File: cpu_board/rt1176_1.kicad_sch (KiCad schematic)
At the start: 40 parts, among them SW1 SWITCH_SMT4.6X2.8, U2 MIMXRT1176

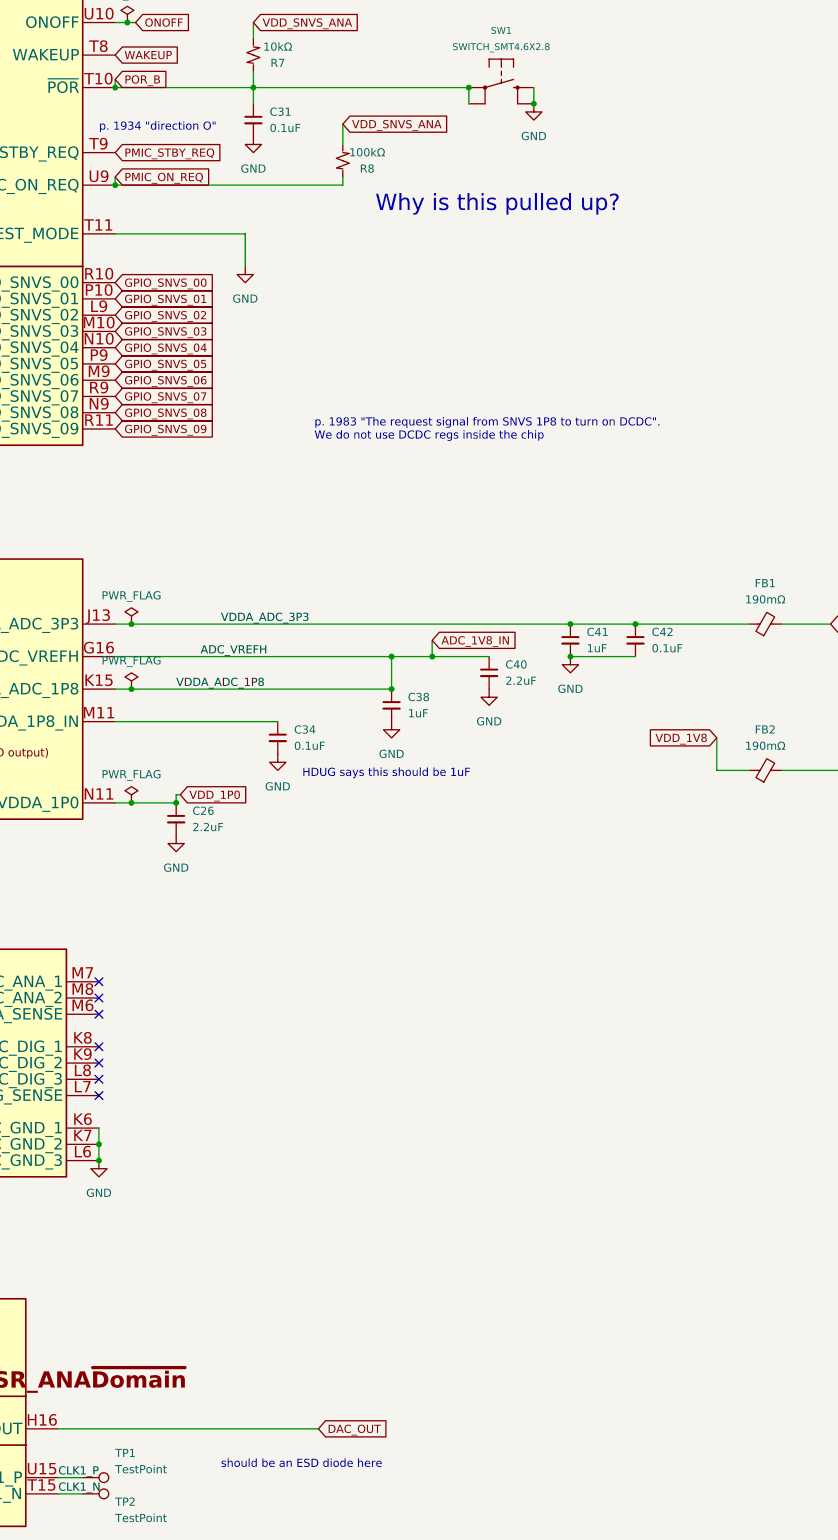
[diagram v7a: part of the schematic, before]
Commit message: move level shifter to top
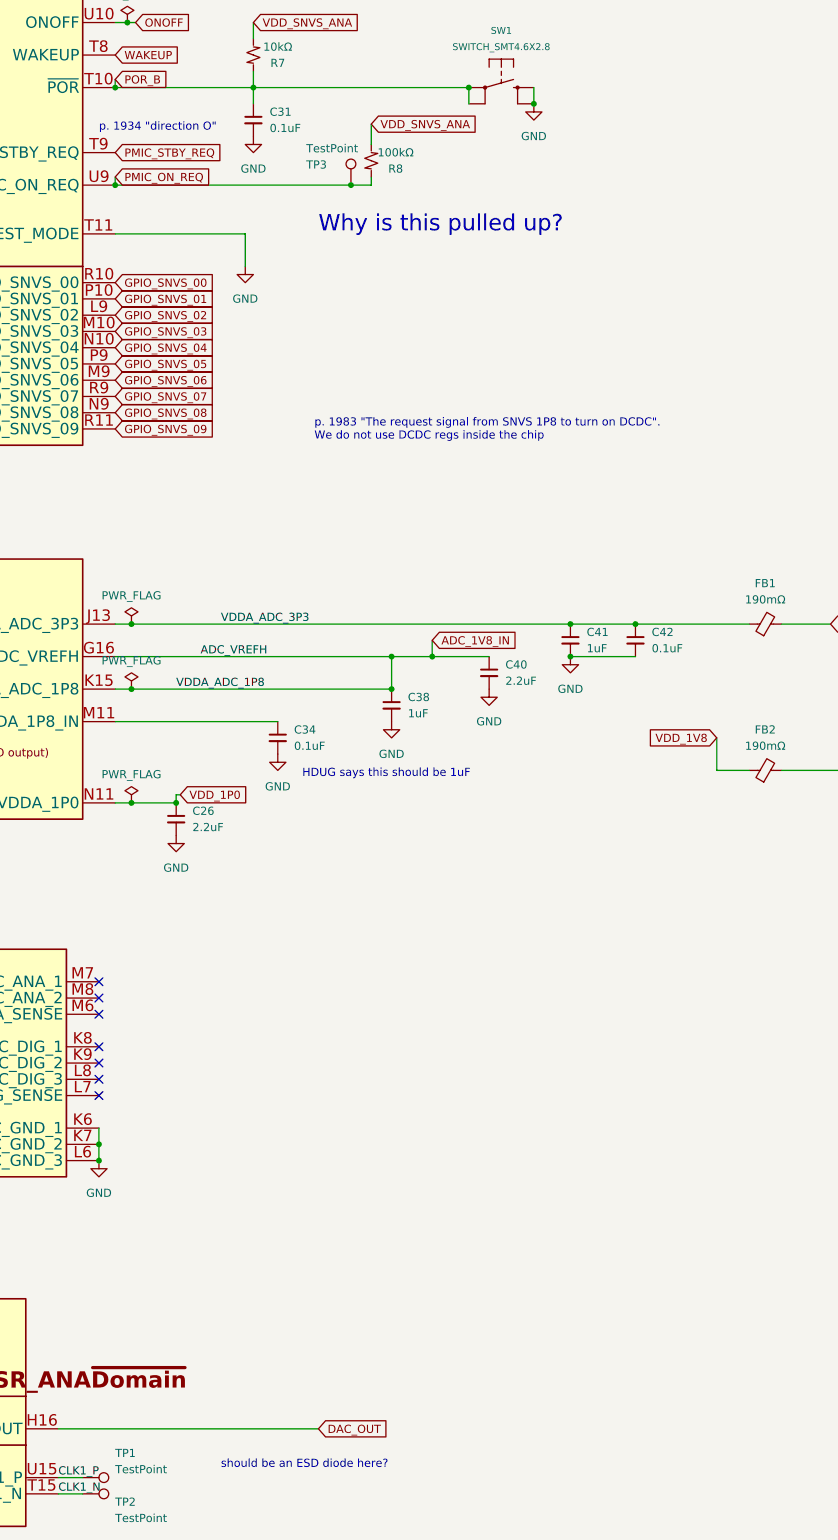
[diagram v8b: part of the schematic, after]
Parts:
- added TP3: TestPoint, TestPoint:TestPoint_Pad_1.0x1.0mm, symbol Connector:TestPoint
- C4: footprint adcs:Perfect_0402 -> Capacitor_SMD:C_0603_1608Metric
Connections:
- net PMIC_ON_REQ: now also TP3.1
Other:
- note added: "should be an ESD diode here?"
- note removed: "should be an ESD diode here"
- moved on the sheet: R8
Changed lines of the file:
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@@
   (junction (at 192.405 40.64) (diameter 0) (color 0 0 0 0)
   )
+  (junction (at 285.75 60.96) (diameter 0) (color 0 0 0 0)
+  )
   (junction (at 35.56 220.98) (diameter 0) (color 0 0 0 0)
   )
@@
     (stroke (width 0) (type default))
   )
+  (wire (pts (xy 248.92 60.96) (xy 285.75 60.96))
+    (stroke (width 0) (type default))
+  )
+  (wire (pts (xy 285.75 60.96) (xy 288.925 60.96))
+    (stroke (width 0) (type default))
+  )
   (wire (pts (xy 193.04 154.94) (xy 193.04 157.48))
     (stroke (width 0) (type default))
@@
     (stroke (width 0) (type default))
   )
-  (wire (pts (xy 284.48 59.69) (xy 284.48 60.96))
+  (wire (pts (xy 288.925 59.69) (xy 288.925 60.96))
     (stroke (width 0) (type default))
   )
@@
     (stroke (width 0) (type default))
   )
-  (wire (pts (xy 284.48 51.435) (xy 284.48 54.61))
+  (wire (pts (xy 288.925 51.435) (xy 288.925 54.61))
     (stroke (width 0) (type default))
   )
@@
     (stroke (width 0) (type default))
   )
-  (wire (pts (xy 248.92 60.96) (xy 284.48 60.96))
-    (stroke (width 0) (type default))
-  )
   (wire (pts (xy 251.46 129.54) (xy 320.04 129.54))
     (stroke (width 0) (type default))
@@
     (effects (font (size 1.27 1.27)) (justify left bottom))
   )
-  (text "should be an ESD diode here\n" (at 265.43 261.62 0)
+  (text "should be an ESD diode here?\n" (at 265.43 261.62 0)
     (effects (font (size 1.27 1.27)) (justify left bottom))
   )
@@
     (effects (font (size 1.27 1.27)) (justify left bottom))
   )
-  (text "Why is this pulled up?" (at 289.56 65.405 0)
+  (text "Why is this pulled up?" (at 280.67 68.58 0)
     (effects (font (size 2.54 2.54) (color 255 0 0 1)) (justify left bottom))
   )
@@
     )
   )
-  (global_label "VDD_SNVS_ANA" (shape input) (at 284.48 51.435 0) (fields_autoplaced)
+  (global_label "VDD_SNVS_ANA" (shape input) (at 288.925 51.435 0) (fields_autoplaced)
     (effects (font (size 1.27 1.27)) (justify left))
-    (property "Intersheetrefs" "${INTERSHEET_REFS}" (at 301.3748 51.435 0)
+    (property "Intersheetrefs" "${INTERSHEET_REFS}" (at 305.8198 51.435 0)
       (effects (font (size 1.27 1.27)) (justify left) hide)
     )
@@
     )
   )
-  (symbol (lib_id "Device:R_Small_US") (at 284.48 57.15 180) (unit 1)
+  (symbol (lib_id "Device:R_Small_US") (at 288.925 57.15 180) (unit 1)
     (in_bom yes) (on_board yes) (dnp no)
-    (property "Reference" "R8" (at 288.29 58.42 0)
+    (property "Reference" "R8" (at 292.735 58.42 0)
       (effects (font (size 1.27 1.27)))
     )
-    (property "Value" "100kΩ" (at 288.29 55.88 0)
+    (property "Value" "100kΩ" (at 292.735 55.88 0)
       (effects (font (size 1.27 1.27)))
     )
-    (property "Footprint" "adcs:Perfect_0402" (at 284.48 57.15 0)
+    (property "Footprint" "adcs:Perfect_0402" (at 288.925 57.15 0)
       (effects (font (size 1.27 1.27)) hide)
     )
-    (property "Datasheet" "" (at 284.48 57.15 0)
+    (property "Datasheet" "" (at 288.925 57.15 0)
       (effects (font (size 1.27 1.27)) hide)
     )
-    (property "JLCPCB P/N" "" (at 284.48 57.15 0)
+    (property "JLCPCB P/N" "" (at 288.925 57.15 0)
       (effects (font (size 1.27 1.27)) hide)
     )
-    (property "JLCPCB P/N Proto" "" (at 284.48 57.15 0)
+    (property "JLCPCB P/N Proto" "" (at 288.925 57.15 0)
       (effects (font (size 1.27 1.27)) hide)
     )
-    (property "Footprint (for JLCPCB)" "0402" (at 284.48 57.15 0)
+    (property "Footprint (for JLCPCB)" "0402" (at 288.925 57.15 0)
       (effects (font (size 1.27 1.27)) hide)
     )
@@
       (effects (font (size 1.27 1.27)) (justify left))
     )
-    (property "Footprint" "adcs:Perfect_0402" (at 121.92 160.02 0)
+    (property "Footprint" "Capacitor_SMD:C_0603_1608Metric" (at 121.92 160.02 0)
       (effects (font (size 1.27 1.27)) hide)
     )
@@
         )
       )
+    )
+  )
+  (symbol (lib_id "Connector:TestPoint") (at 285.75 60.96 0) (unit 1)
+    (in_bom yes) (on_board yes) (dnp no)
+    (property "Reference" "TP3" (at 278.765 57.785 0)
+      (effects (font (size 1.27 1.27)) (justify left))
+    )
+    (property "Value" "TestPoint" (at 278.765 55.245 0)
+      (effects (font (size 1.27 1.27)) (justify left))
+    )
+    (property "Footprint" "TestPoint:TestPoint_Pad_1.0x1.0mm" (at 290.83 60.96 0)
+      (effects (font (size 1.27 1.27)) hide)
+    )
+    (property "Datasheet" "~" (at 290.83 60.96 0)
+      (effects (font (size 1.27 1.27)) hide)
+    )
+    (property "Description" "Testpoints" (at 285.75 60.96 0)
+      (effects (font (size 1.27 1.27)) hide)
+    )
+    (property "JLCPCB P/N" "C221678" (at 285.75 60.96 0)
+      (effects (font (size 1.27 1.27)) hide)
+    )
+    (property "JLCPCB P/N Proto" "" (at 285.75 60.96 0)
+      (effects (font (size 1.27 1.27)) hide)
+    )
+    (property "DNI" "DNI" (at 285.75 60.96 0)
+      (effects (font (size 1.27 1.27)) hide)
+    )
+    (property "Footprint (for JLCPCB)" "" (at 285.75 60.96 0)
+      (effects (font (size 1.27 1.27)) hide)
+    )
+    (pin "1")
+    (instances
+      (project "cpu_board"
+        (path "/c4fd7bdd-408e-44be-b66f-e6a18a0ca6e3/9cbcd73e-afcb-4ff3-8583-4372f7e826ca"
+          (reference "TP3") (unit 1)
+        )
+      )
